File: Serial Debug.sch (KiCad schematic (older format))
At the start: 16 parts

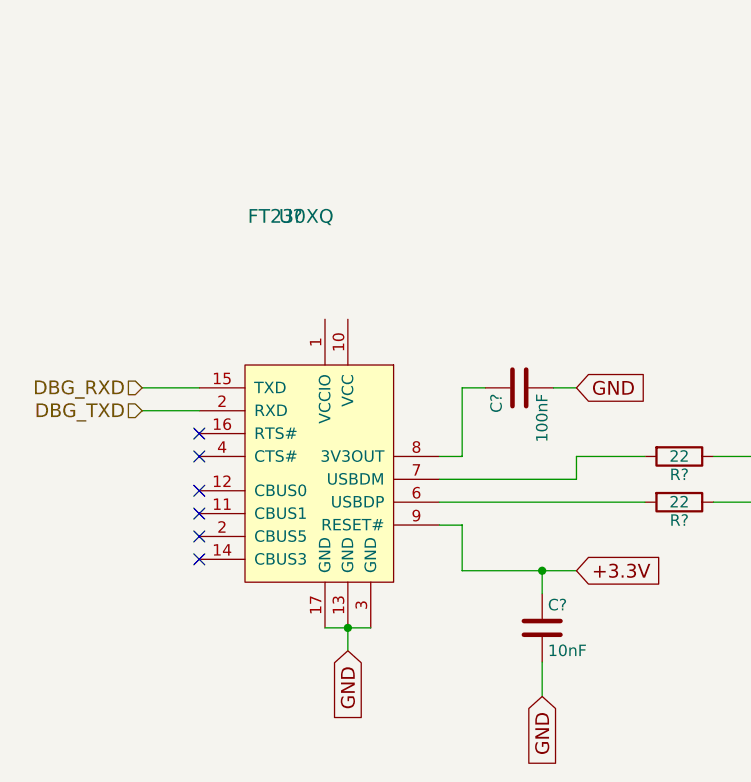
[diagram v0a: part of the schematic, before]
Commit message: I have forgotten to add power to the usb converter chip
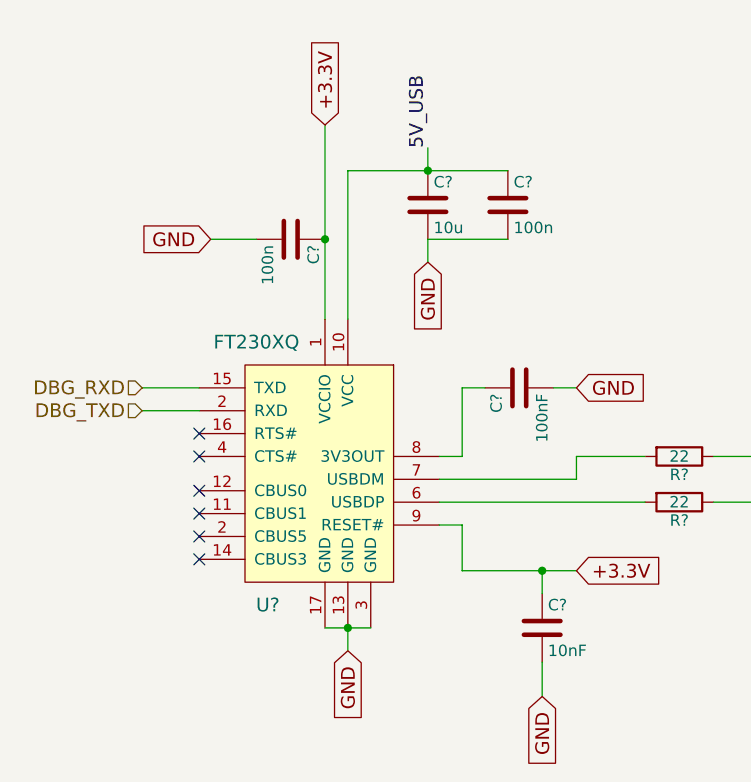
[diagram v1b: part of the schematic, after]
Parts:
- added C?: 10u, symbol C
- added C? (x2): 100n, symbol C
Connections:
- net +3.3V: now also U?.1 (VCCIO), C?.1
- net 5V_USB: now also U?.10 (VCC), C?.1, C?.1
- net GND: now also C?.2, C?.2, C?.2
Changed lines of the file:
@@
 U 1 1 59A28254
 P 2450 2100
-F 0 "U?" H 2450 2100 60  0000 C CNN
-F 1 "FT230XQ" H 2450 2100 60  0000 C CNN
+F 0 "U?" H 2550 400 60  0000 C CNN
+F 1 "FT230XQ" H 2600 1550 60  0000 C CNN
 F 2 "" H 2450 2100 60  0001 C CNN
 F 3 "" H 2450 2100 60  0001 C CNN
@@
 Wire Wire Line
 	8500 5350 8500 5500
+Text Label 3050 1800 1    60   ~ 0
+5V_USB
+$Comp
+L C C?
+U 1 1 59A63DF8
+P 3050 2050
+F 0 "C?" H 3075 2150 50  0000 L CNN
+F 1 "10u" H 3075 1950 50  0000 L CNN
+F 2 "" H 3088 1900 50  0001 C CNN
+F 3 "" H 3050 2050 50  0001 C CNN
+	1    3050 2050
+	1    0    0    -1
+$EndComp
+$Comp
+L C C?
+U 1 1 59A63E5E
+P 3400 2050
+F 0 "C?" H 3425 2150 50  0000 L CNN
+F 1 "100n" H 3425 1950 50  0000 L CNN
+F 2 "" H 3438 1900 50  0001 C CNN
+F 3 "" H 3400 2050 50  0001 C CNN
+	1    3400 2050
+	1    0    0    -1
+$EndComp
+Text GLabel 3050 2300 3    60   Input ~ 0
+GND
+Wire Wire Line
+	3050 2200 3050 2300
+Wire Wire Line
+	3050 2200 3400 2200
+Wire Wire Line
+	2700 1900 3400 1900
+Wire Wire Line
+	3050 1900 3050 1800
+Wire Wire Line
+	2700 1900 2700 2550
+Connection ~ 3050 1900
+Text GLabel 2600 1700 1    60   Input ~ 0
++3.3V
+$Comp
+L C C?
+U 1 1 59A64E99
+P 2450 2200
+F 0 "C?" H 2475 2300 50  0000 L CNN
+F 1 "100n" H 2475 2100 50  0000 L CNN
+F 2 "" H 2488 2050 50  0001 C CNN
+F 3 "" H 2450 2200 50  0001 C CNN
+	1    2450 2200
+	0    1    1    0
+$EndComp
+Wire Wire Line
+	2600 1700 2600 2550
+Wire Wire Line
+	2300 2200 2100 2200
+Connection ~ 2600 2200
+Text GLabel 2100 2200 0    60   Input ~ 0
+GND
 $EndSCHEMATC

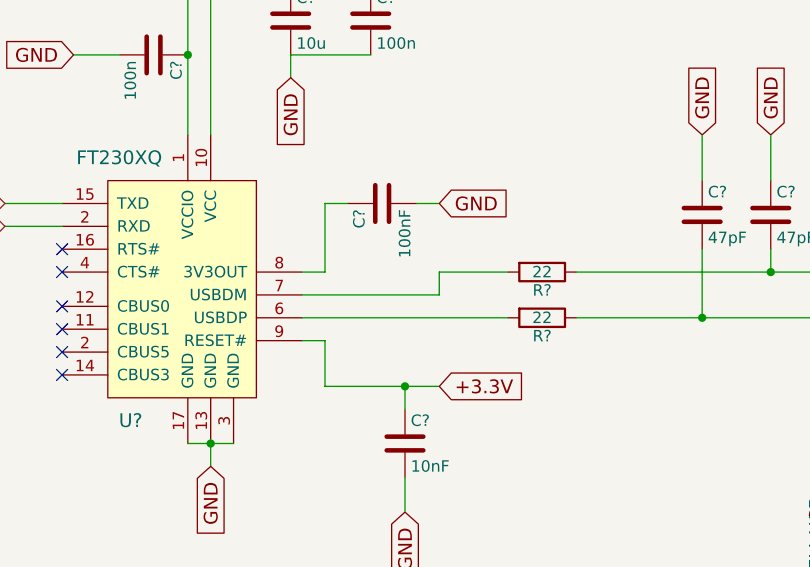
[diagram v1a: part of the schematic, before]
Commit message: feature complete; the next step is the verification of the values and the schematics
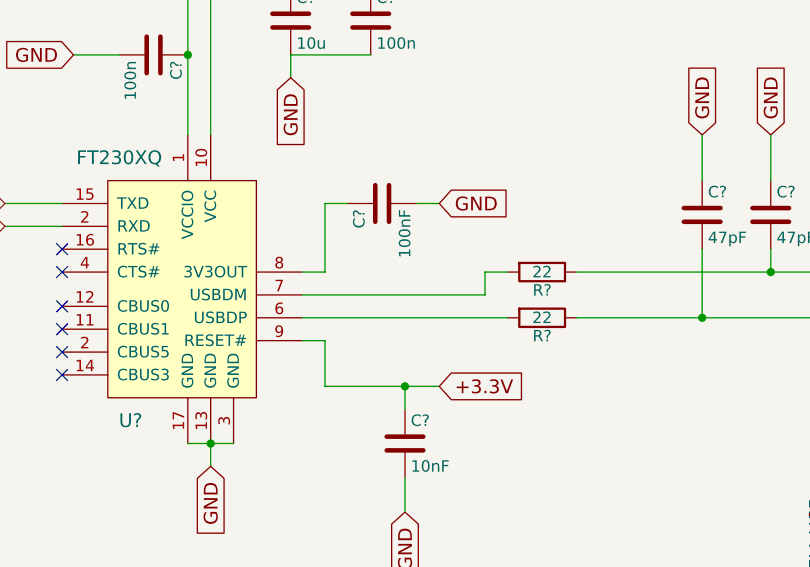
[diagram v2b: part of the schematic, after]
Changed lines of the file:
@@
 	4300 3150 5550 3150
 Wire Wire Line
-	4000 3150 3700 3150
-Wire Wire Line
-	3700 3150 3700 3250
-Wire Wire Line
-	3700 3250 3100 3250
+	3100 3250 3900 3250
 $Comp
 L USB_OTG J?
@@
 Text GLabel 2100 2200 0    60   Input ~ 0
 GND
+Wire Wire Line
+	3900 3250 3900 3150
+Wire Wire Line
+	3900 3150 4000 3150
 $EndSCHEMATC

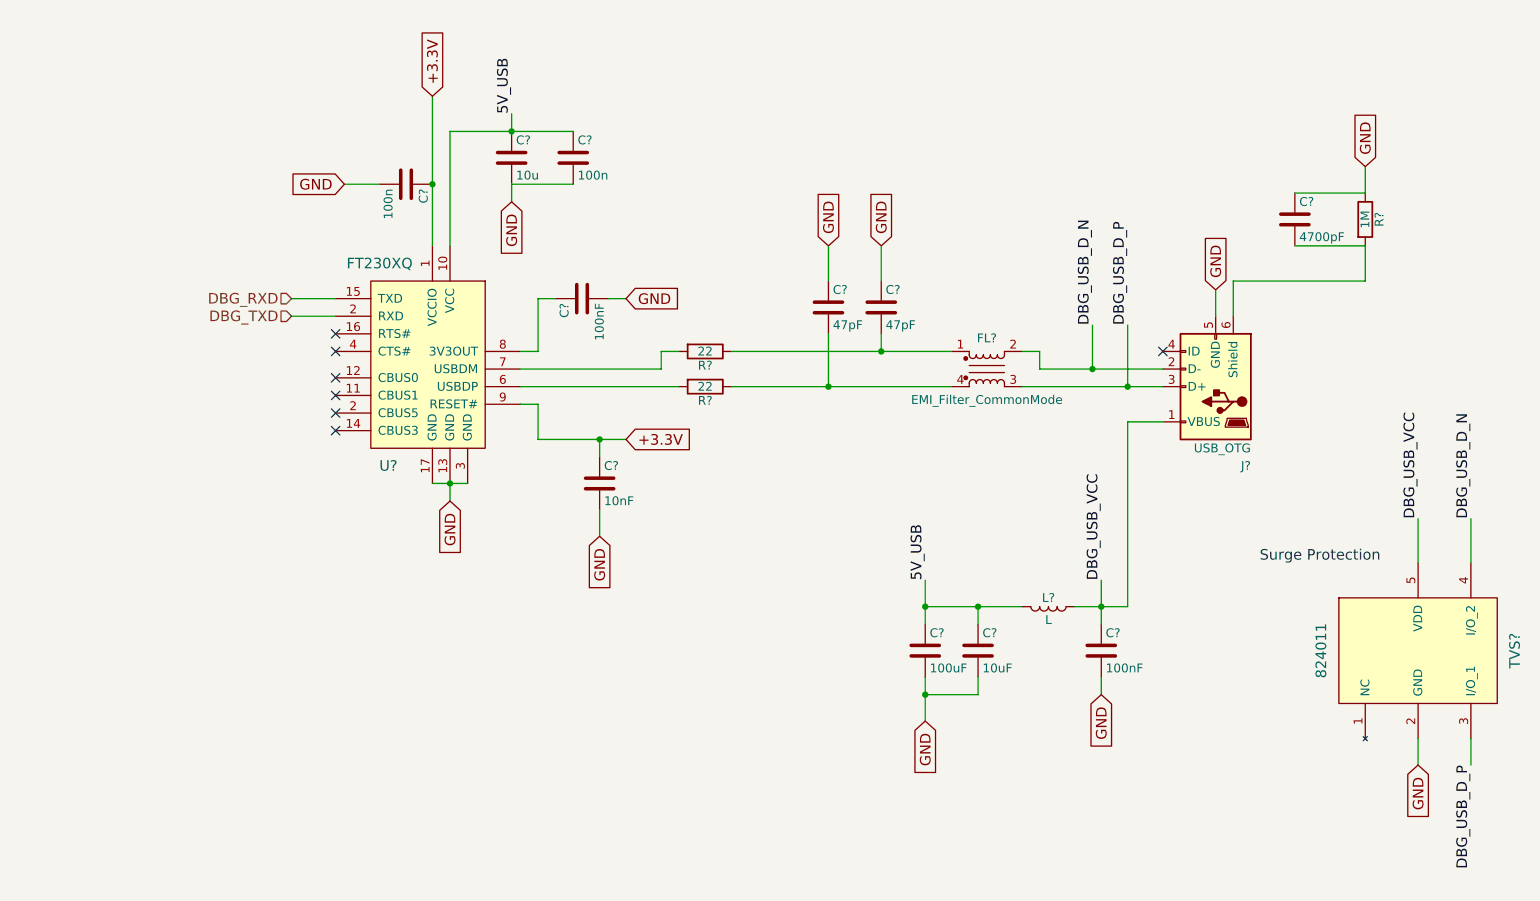
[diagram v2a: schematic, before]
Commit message: this version contains the datasheets and the footprints of the parts
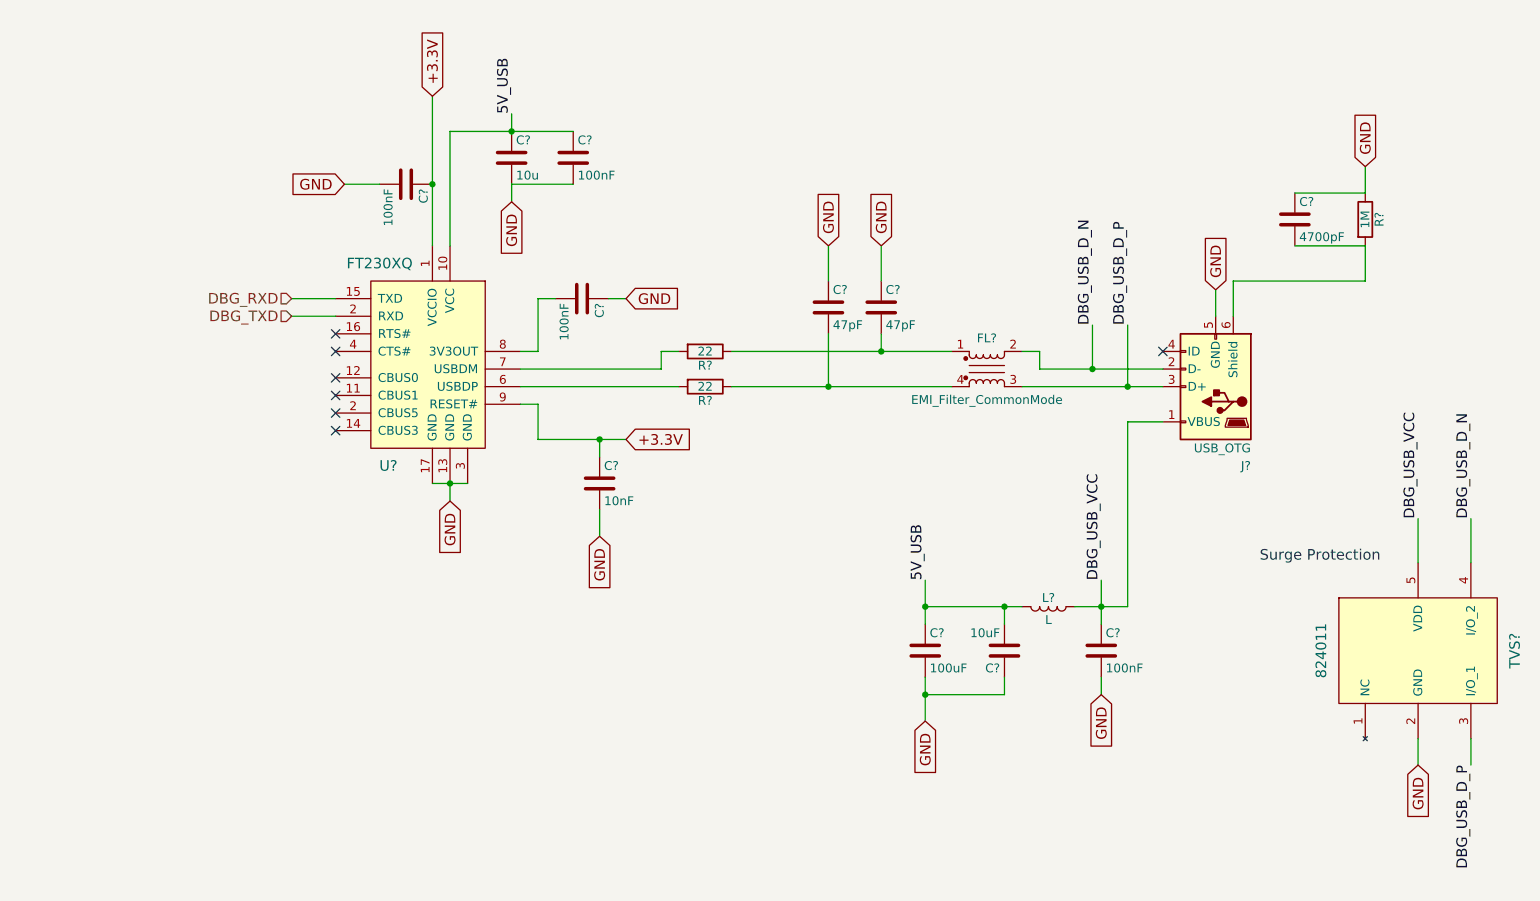
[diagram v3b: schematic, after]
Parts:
- removed C? (x2): 100nF, symbol C
- removed C?: 10nF, symbol C
- removed C?: 10uF, symbol C
- removed C? (x2): 100n, symbol C
- added C?: 10nF, Capacitors_SMD:C_0603_HandSoldering, symbol C
- added C? (x4): 100nF, Capacitors_SMD:C_0603_HandSoldering, symbol C
- added C?: 10uF, Capacitors_SMD:C_0603_HandSoldering, symbol C
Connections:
- net +3.3V: now also C?.1, C?.1
- net 5V_USB: now also C?.1, C?.2
- net DBG_USB_VCC: now also C?.1
- net GND: now also C?.1, C?.1, C?.2, C?.2, C?.2, C?.2
- net at U?.8 (3V3OUT): now also C?.2
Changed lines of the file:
@@
 	-1   0    0    -1
-$EndComp
-$Comp
-L C C?
-U 1 1 59A282CA
-P 3450 2850
-F 0 "C?" H 3475 2950 50  0000 L CNN
-F 1 "100nF" H 3475 2750 50  0000 L CNN
-F 2 "" H 3488 2700 50  0001 C CNN
-F 3 "" H 3450 2850 50  0001 C CNN
-	1    3450 2850
-	0    -1   1    0
 $EndComp
 Text GLabel 3700 2850 2    60   Input ~ 0
@@
 Text GLabel 3700 3650 2    60   Input ~ 0
 +3.3V
-$Comp
-L C C?
-U 1 1 59A29C3F
-P 3550 3900
-F 0 "C?" H 3575 4000 50  0000 L CNN
-F 1 "10nF" H 3575 3800 50  0000 L CNN
-F 2 "" H 3588 3750 50  0001 C CNN
-F 3 "" H 3550 3900 50  0001 C CNN
-	1    3550 3900
-	1    0    0    -1
-$EndComp
 Text GLabel 3550 4200 3    60   Input ~ 0
 GND
@@
 $EndComp
 $Comp
-L C C?
-U 1 1 59A2D039
-P 5700 4850
-F 0 "C?" H 5725 4950 50  0000 L CNN
-F 1 "10uF" H 5725 4750 50  0000 L CNN
-F 2 "" H 5738 4700 50  0001 C CNN
-F 3 "" H 5700 4850 50  0001 C CNN
-	1    5700 4850
-	1    0    0    -1
-$EndComp
-$Comp
-L C C?
-U 1 1 59A2D064
-P 6400 4850
-F 0 "C?" H 6425 4950 50  0000 L CNN
-F 1 "100nF" H 6425 4750 50  0000 L CNN
-F 2 "" H 6438 4700 50  0001 C CNN
-F 3 "" H 6400 4850 50  0001 C CNN
-	1    6400 4850
-	1    0    0    -1
-$EndComp
-$Comp
 L L L?
 U 1 1 59A2D09D
@@
 	5400 4600 5950 4600
 Wire Wire Line
-	5700 4700 5700 4600
-Connection ~ 5700 4600
-Wire Wire Line
 	6400 4450 6400 4700
 Wire Wire Line
@@
 	5400 5000 5400 5250
 Wire Wire Line
-	5400 5100 5700 5100
-Wire Wire Line
-	5700 5100 5700 5000
+	5400 5100 5850 5100
 Text GLabel 6400 5100 3    60   Input ~ 0
 GND
@@
 	1    0    0    -1
 $EndComp
-$Comp
-L C C?
-U 1 1 59A63E5E
-P 3400 2050
-F 0 "C?" H 3425 2150 50  0000 L CNN
-F 1 "100n" H 3425 1950 50  0000 L CNN
-F 2 "" H 3438 1900 50  0001 C CNN
-F 3 "" H 3400 2050 50  0001 C CNN
-	1    3400 2050
-	1    0    0    -1
-$EndComp
 Text GLabel 3050 2300 3    60   Input ~ 0
 GND
@@
 Text GLabel 2600 1700 1    60   Input ~ 0
 +3.3V
-$Comp
-L C C?
-U 1 1 59A64E99
-P 2450 2200
-F 0 "C?" H 2475 2300 50  0000 L CNN
-F 1 "100n" H 2475 2100 50  0000 L CNN
-F 2 "" H 2488 2050 50  0001 C CNN
-F 3 "" H 2450 2200 50  0001 C CNN
-	1    2450 2200
-	0    1    1    0
-$EndComp
 Wire Wire Line
 	2600 1700 2600 2550
@@
 Wire Wire Line
 	3900 3150 4000 3150
+$Comp
+L C C?
+U 1 1 59A86400
+P 5850 4850
+F 0 "C?" H 5875 4950 50  0000 L CNN
+F 1 "10uF" H 5875 4750 50  0000 L CNN
+F 2 "Capacitors_SMD:C_0603_HandSoldering" H 5888 4700 30  0001 C CNN
+F 3 "http://hu.farnell.com/murata/grm188r60g106me47d/cap-mlcc-x5r-10uf-4v-0603/dp/2688517" H 5850 4850 60  0001 C CNN
+F 4 "http://hu.farnell.com/avx/06036d106mat2a/cap-mlcc-x5r-10uf-6-3v-0603/dp/1833804" H 5850 4850 60  0001 C CNN "avx"
+	1    5850 4850
+	-1   0    0    1
+$EndComp
+Wire Wire Line
+	5850 5100 5850 5000
+Wire Wire Line
+	5850 4700 5850 4600
+Connection ~ 5850 4600
+$Comp
+L C C?
+U 1 1 59A67671
+P 3550 3900
+F 0 "C?" H 3575 4000 50  0000 L CNN
+F 1 "10nF" H 3575 3800 50  0000 L CNN
+F 2 "Capacitors_SMD:C_0603_HandSoldering" H 3588 3750 50  0001 C CNN
+F 3 "http://hu.farnell.com/multicomp/mc0603b103k500ct/cap-mlcc-x7r-10nf-50v-0603/dp/1759102" H 3550 3900 50  0001 C CNN
+	1    3550 3900
+	1    0    0    -1
+$EndComp
+$Comp
+L C C?
+U 1 1 59A67F9E
+P 3450 2850
+F 0 "C?" H 3475 2950 50  0000 L CNN
+F 1 "100nF" H 3475 2750 50  0000 L CNN
+F 2 "Capacitors_SMD:C_0603_HandSoldering" H 3488 2700 30  0001 C CNN
+F 3 "hu.farnell.com/avx/06035c104kat2a/cap-mlcc-x7r-100nf-50v-0603/dp/1301804" H 3450 2850 60  0001 C CNN
+	1    3450 2850
+	0    1    1    0
+$EndComp
+$Comp
+L C C?
+U 1 1 59A68788
+P 6400 4850
+F 0 "C?" H 6425 4950 50  0000 L CNN
+F 1 "100nF" H 6425 4750 50  0000 L CNN
+F 2 "Capacitors_SMD:C_0603_HandSoldering" H 6438 4700 30  0001 C CNN
+F 3 "hu.farnell.com/avx/06035c104kat2a/cap-mlcc-x7r-100nf-50v-0603/dp/1301804" H 6400 4850 60  0001 C CNN
+	1    6400 4850
+	1    0    0    -1
+$EndComp
+$Comp
+L C C?
+U 1 1 59A68F5E
+P 3400 2050
+F 0 "C?" H 3425 2150 50  0000 L CNN
+F 1 "100nF" H 3425 1950 50  0000 L CNN
+F 2 "Capacitors_SMD:C_0603_HandSoldering" H 3438 1900 30  0001 C CNN
+F 3 "hu.farnell.com/avx/06035c104kat2a/cap-mlcc-x7r-100nf-50v-0603/dp/1301804" H 3400 2050 60  0001 C CNN
+	1    3400 2050
+	1    0    0    -1
+$EndComp
+$Comp
+L C C?
+U 1 1 59A69729
+P 2450 2200
+F 0 "C?" H 2475 2300 50  0000 L CNN
+F 1 "100nF" H 2475 2100 50  0000 L CNN
+F 2 "Capacitors_SMD:C_0603_HandSoldering" H 2488 2050 30  0001 C CNN
+F 3 "hu.farnell.com/avx/06035c104kat2a/cap-mlcc-x7r-100nf-50v-0603/dp/1301804" H 2450 2200 60  0001 C CNN
+	1    2450 2200
+	0    1    1    0
+$EndComp
 $EndSCHEMATC
